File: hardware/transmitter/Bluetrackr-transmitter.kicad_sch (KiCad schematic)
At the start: 59 parts, among them J1 USB_C_Receptacle_USB2.0, J2 Programming_Connector, J3 Battery_Connector, Q1 CJ2333, Q2 BSS138, Q3 BSS138, Q4 BSS138, Q5 BSS138, Q6 BSS138, SW1 SW_Pair, U1 MCP73831-2-OT, U2 MIC5205-2.5YM5, U3 MCP1700-1802E_SOT23, U4 STM32F030R8Tx, U6 ICM-20948

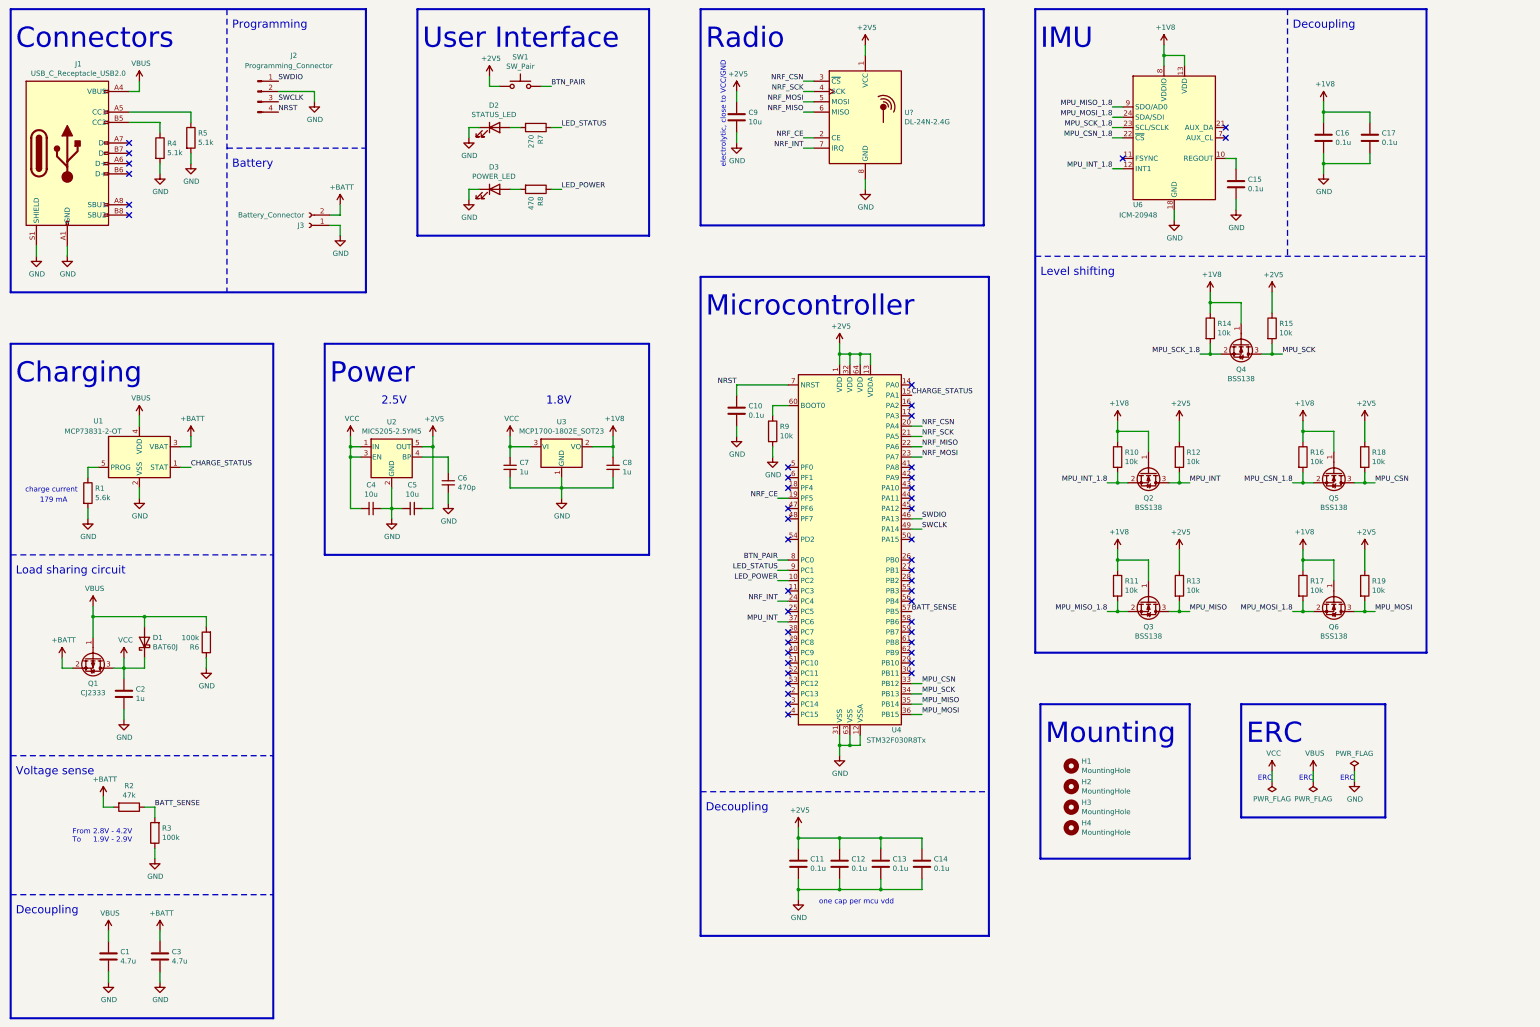
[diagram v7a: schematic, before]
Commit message: Replace ICM-20948 with LSM9DS1, removes 1.8V supply and level shifters
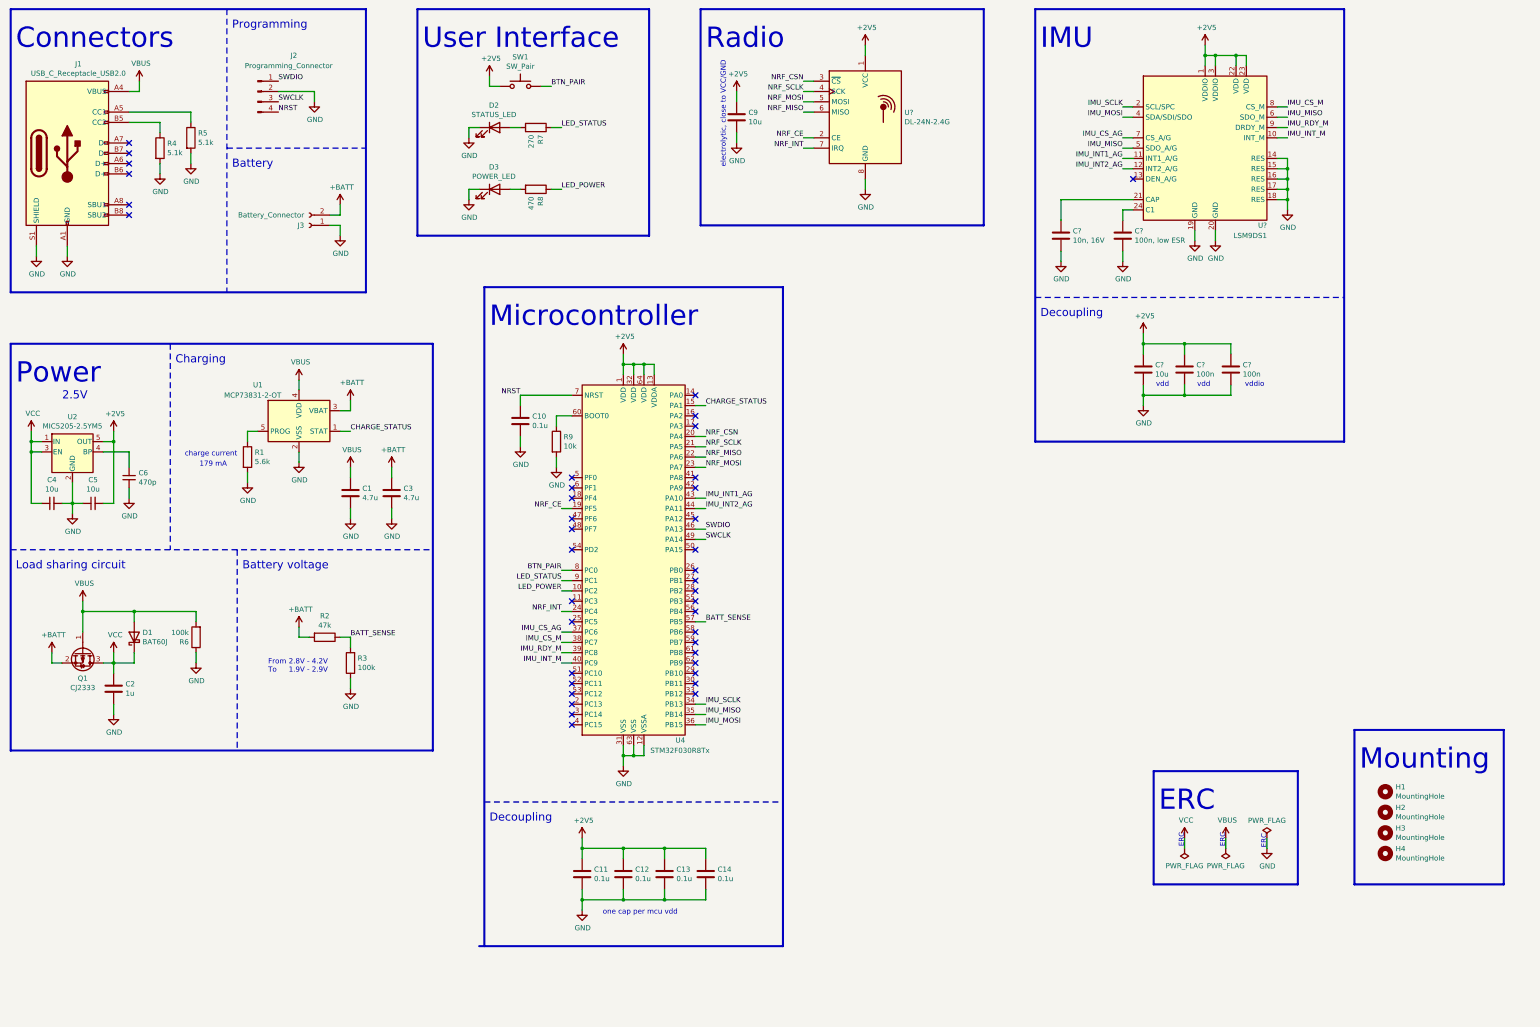
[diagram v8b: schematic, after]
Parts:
- removed C15, C16, C17: 0.1u, Capacitor_SMD:C_0805_2012Metric_Pad1.15x1.40mm_HandSolder, symbol Device:C
- removed C7, C8: 1u, Capacitor_SMD:C_0805_2012Metric_Pad1.15x1.40mm_HandSolder, symbol Device:C_Small
- removed Q2, Q3, Q4, Q5, Q6: BSS138, Package_TO_SOT_SMD:SOT-23, symbol Transistor_FET:BSS138
- removed R10, R11, R12, R13, R14, R15, R16, R17, R18, R19: 10k, Resistor_SMD:R_0805_2012Metric_Pad1.15x1.40mm_HandSolder, symbol Device:R
- removed U3: MCP1700-1802E_SOT23, Package_TO_SOT_SMD:SOT-23, symbol Regulator_Linear:MCP1700-1802E_SOT23
- removed U6: ICM-20948, Sensor_Motion:InvenSense_QFN-24_3x3mm_P0.4mm, symbol Sensor_Motion:ICM-20948
- added C?: 100n, low ESR, symbol Device:C
- added C?: 10u, symbol Device:C
- added C?: 10n, 16V, symbol Device:C
- added C? (x2): 100n, symbol Device:C
- added U?: LSM9DS1, Package_LGA:LGA-24L_3x3.5mm_P0.43mm, symbol Sensor_Motion:LSM9DS1
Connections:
- net +2V5: now also C?.1, C?.1, C?.1, U?.1 (VDDIO), U?.22 (VDD), U?.23 (VDD), U?.3 (VDDIO)
- net GND: now also C?.2, C?.2, C?.2, C?.2, C?.2, U?.14 (RES), U?.15 (RES), U?.16 (RES), U?.17 (RES), U?.18 (RES), U?.19 (GND), U?.20 (GND)
- net IMU_CS_M: now reaches U4.38 (PC7)
- net IMU_CS_M: now also U?.8 (CS_M)
- net IMU_RDY_M: now reaches U4.39 (PC8)
- net IMU_RDY_M: now also U?.9 (DRDY_M)
- net IMU_INT_M: now reaches U4.40 (PC9)
- net IMU_INT_M: now also U?.10 (INT_M)
- net IMU_INT1_AG: now reaches U4.43 (PA10)
- net IMU_INT1_AG: now also U?.11 (INT1_A/G)
- net IMU_INT2_AG: now reaches U4.44 (PA11)
- net IMU_INT2_AG: now also U?.12 (INT2_A/G)
- net MPU_CSN: no longer names the net of U4.33 (PB12)
- net MPU_INT renamed IMU_CS_AG
- net IMU_CS_AG: now also U?.7 (CS_A/G)
- net MPU_MISO renamed IMU_MISO
- net IMU_MISO: now also U?.5 (SDO_A/G), U?.6 (SDO_M)
- net MPU_MOSI renamed IMU_MOSI
- net IMU_MOSI: now also U?.4 (SDA/SDI/SDO)
- net MPU_SCK renamed IMU_SCLK
- net IMU_SCLK: now also U?.2 (SCL/SPC)
- net NRF_SCK renamed NRF_SCLK
- new net: C?.1, U?.24 (C1)
- new net: C?.1, U?.21 (CAP)
- no-connect marks 46 -> 40
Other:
- note added: "Battery voltage"
- note added: "vdd"
- note added: "vddio"
- note removed: "1.8V"
- note removed: "Level shifting"
- note removed: "Voltage sense"
- moved on the sheet: C1, C10, C11, C12, C13, C14, C2, C3, C4, C5, C6, D1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
